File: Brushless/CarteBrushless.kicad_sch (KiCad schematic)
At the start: 65 parts, among them J1 Conn_01x03_Pin, J16 ALIM, J2 Conn_01x03_Pin, J3 Conn_01x03_Pin, Q2 IRF7424, U1 STM32G484RETx, U2 TCAN332G

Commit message: liste des composants
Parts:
- Transfo18->5: Ref RS (none) -> 144-6290
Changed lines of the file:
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@@
+			)
+		)
+		(property "Ref RS" "144-6290"
+			(at 78.74 44.45 0)
+			(effects
+				(font
+					(size 1.27 1.27)
+				)
+				(hide yes)
 			)
 		)

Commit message: composants
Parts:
- C23: Ref RS 766-1104 -> 135-9884
- QUARTZ1: Farnel (none) -> 3573056; RS (none) -> 171-2862
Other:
- note added: "Pour la prochaine itération : - Attention au XT30"
- note removed: "- Check ! - Check !"
- note removed: "VERIFIER: - l'ordre des pins de molex - Les valeurs de resistances de terminaison"
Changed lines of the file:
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@@
 	(text "Valeurs des R_leds marqué \"osef\" (il y en a 3 )\nElles sont reliées à des leds donc on peut les choisir après"
 		(exclude_from_sim no)
-		(at 150.114 165.354 0)
+		(at 108.204 187.706 0)
 		(effects
 			(font
@@
 		)
 	)
-	(text "VERIFIER:\n- l'ordre des pins de molex\n- Les valeurs de resistances\n  de terminaison"
+	(text "Pour la prochaine itération : \n- Attention au XT30"
 		(exclude_from_sim no)
-		(at 108.458 193.802 0)
+		(at 223.52 166.116 0)
 		(effects
 			(font
-				(size 5.08 5.08)
+				(size 3.81 3.81)
 				(thickness 2.54)
 				(bold yes)
@@
 		)
 	)
-	(text "- Check !\n- Check !"
-		(exclude_from_sim no)
-		(at 231.14 185.928 0)
-		(effects
-			(font
-				(size 5.08 5.08)
-				(thickness 2.54)
-				(bold yes)
-				(color 0 194 0 1)
-			)
-			(justify left bottom)
-		)
-	)
 	(text "Connectique USB UART DEBUG"
 		(exclude_from_sim no)
@@
 			)
 		)
-		(property "Ref RS" "    766-1104"
+		(property "Ref RS" "135-9884"
 			(at 69.85 55.88 0)
 			(effects
@@
 			)
 		)
-		(property "Description" ""
+		(property "Description" "Equivalent au IRF7404"
 			(at 43.18 46.99 0)
 			(effects
@@
 			(effects
 				(font
+					(size 1.27 1.27)
+				)
+				(hide yes)
+			)
+		)
+		(property "RS" "171-2862"
+			(at 81.28 173.99 0)
+			(effects
+				(font
+					(size 1.27 1.27)
+				)
+				(hide yes)
+			)
+		)
+		(property "Farnel" "3573056"
+			(at 81.28 173.99 0)
+			(effects
+				(font

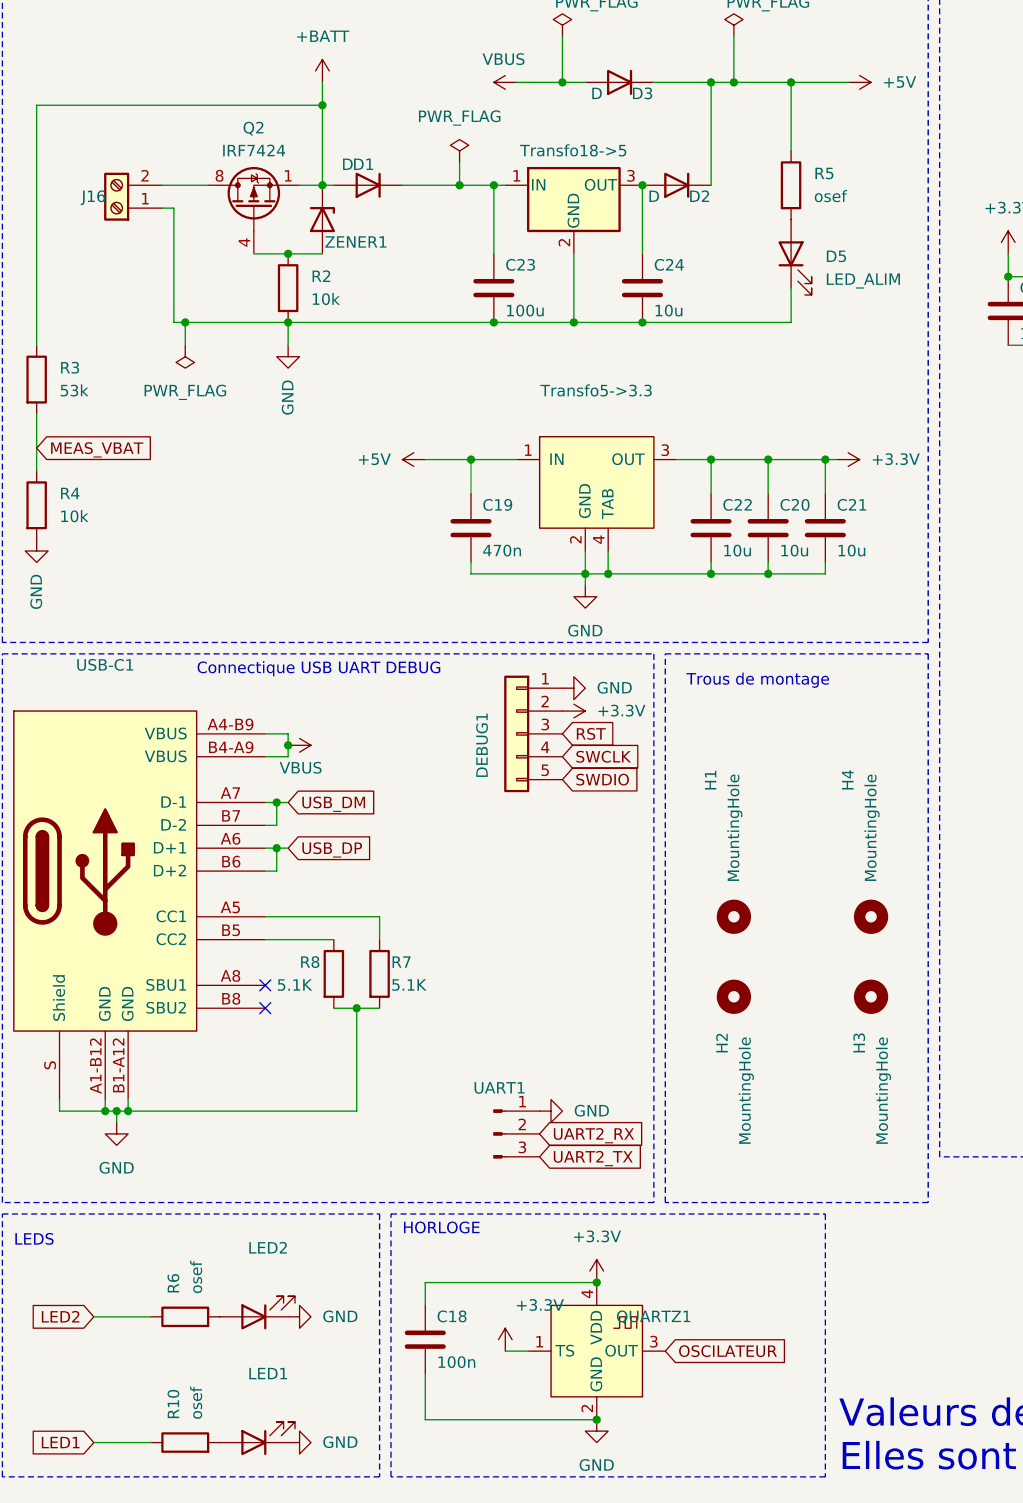
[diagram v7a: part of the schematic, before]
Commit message: resistance LED + schema soudure
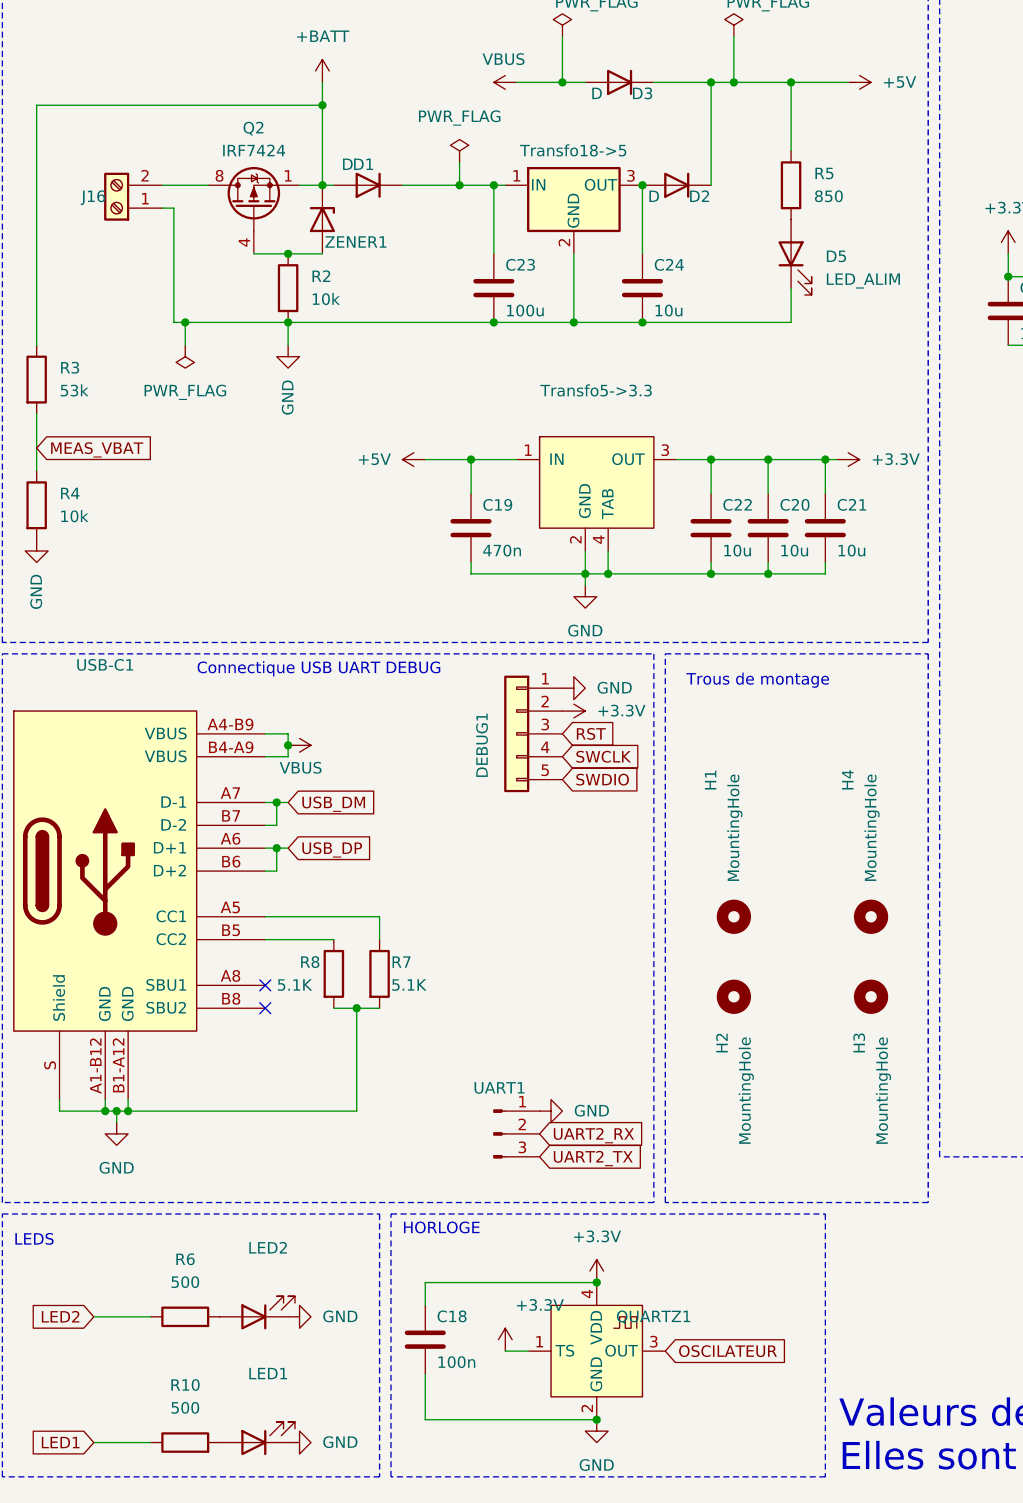
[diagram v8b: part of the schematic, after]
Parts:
- R10, R6: value osef -> 500
- R5: value osef -> 850
